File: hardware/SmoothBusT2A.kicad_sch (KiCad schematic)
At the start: 6 parts, among them U1 ATTINY85-20SU, U2 MC7805BDTRKG

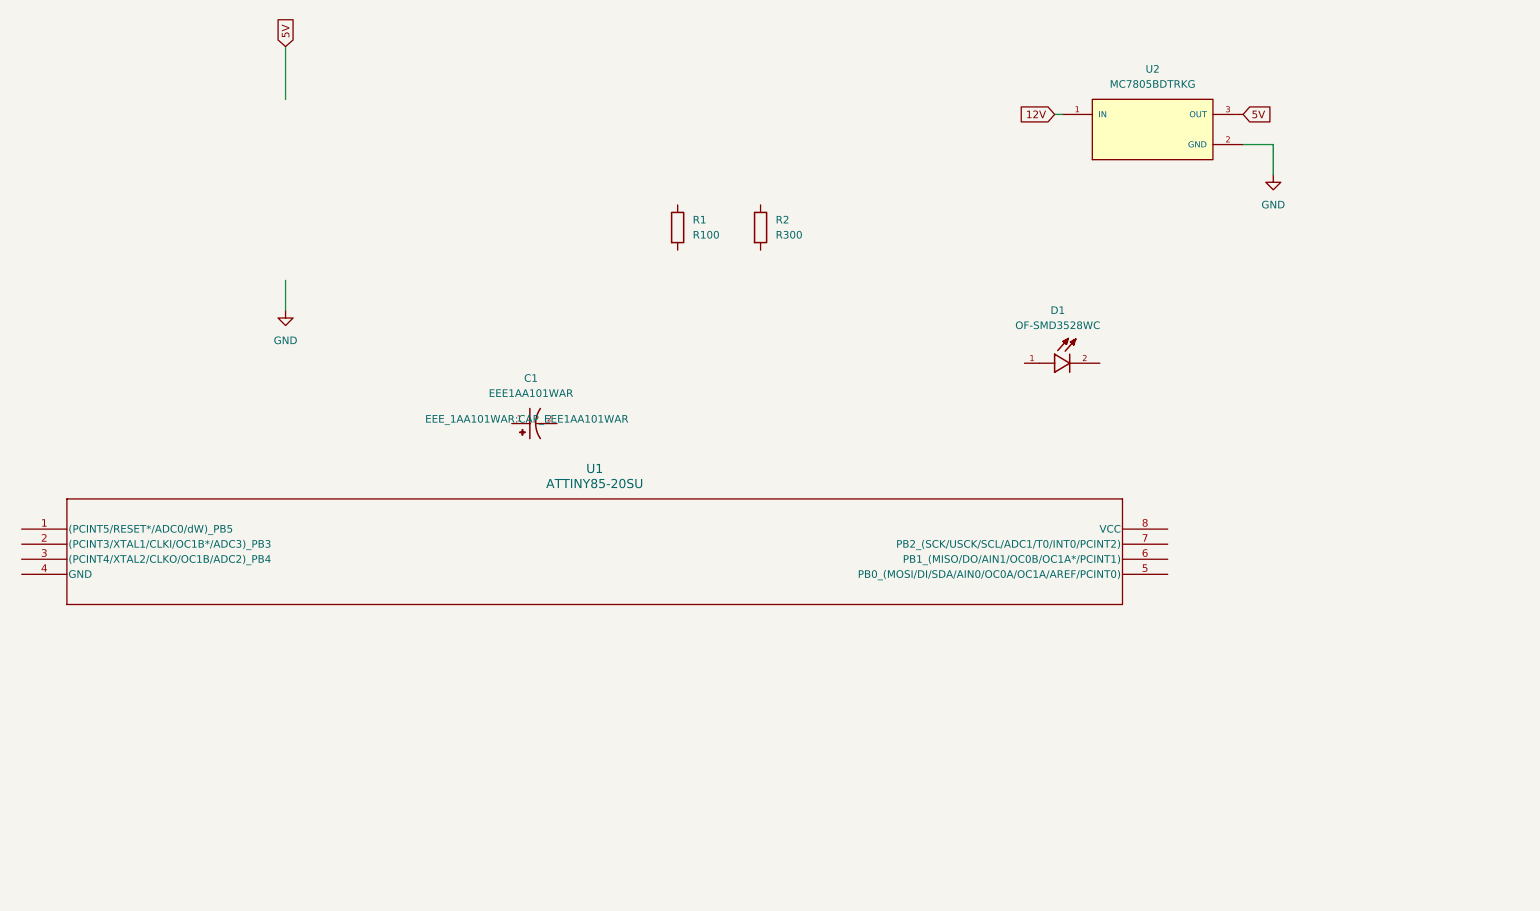
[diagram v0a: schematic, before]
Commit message: added parts to pcb
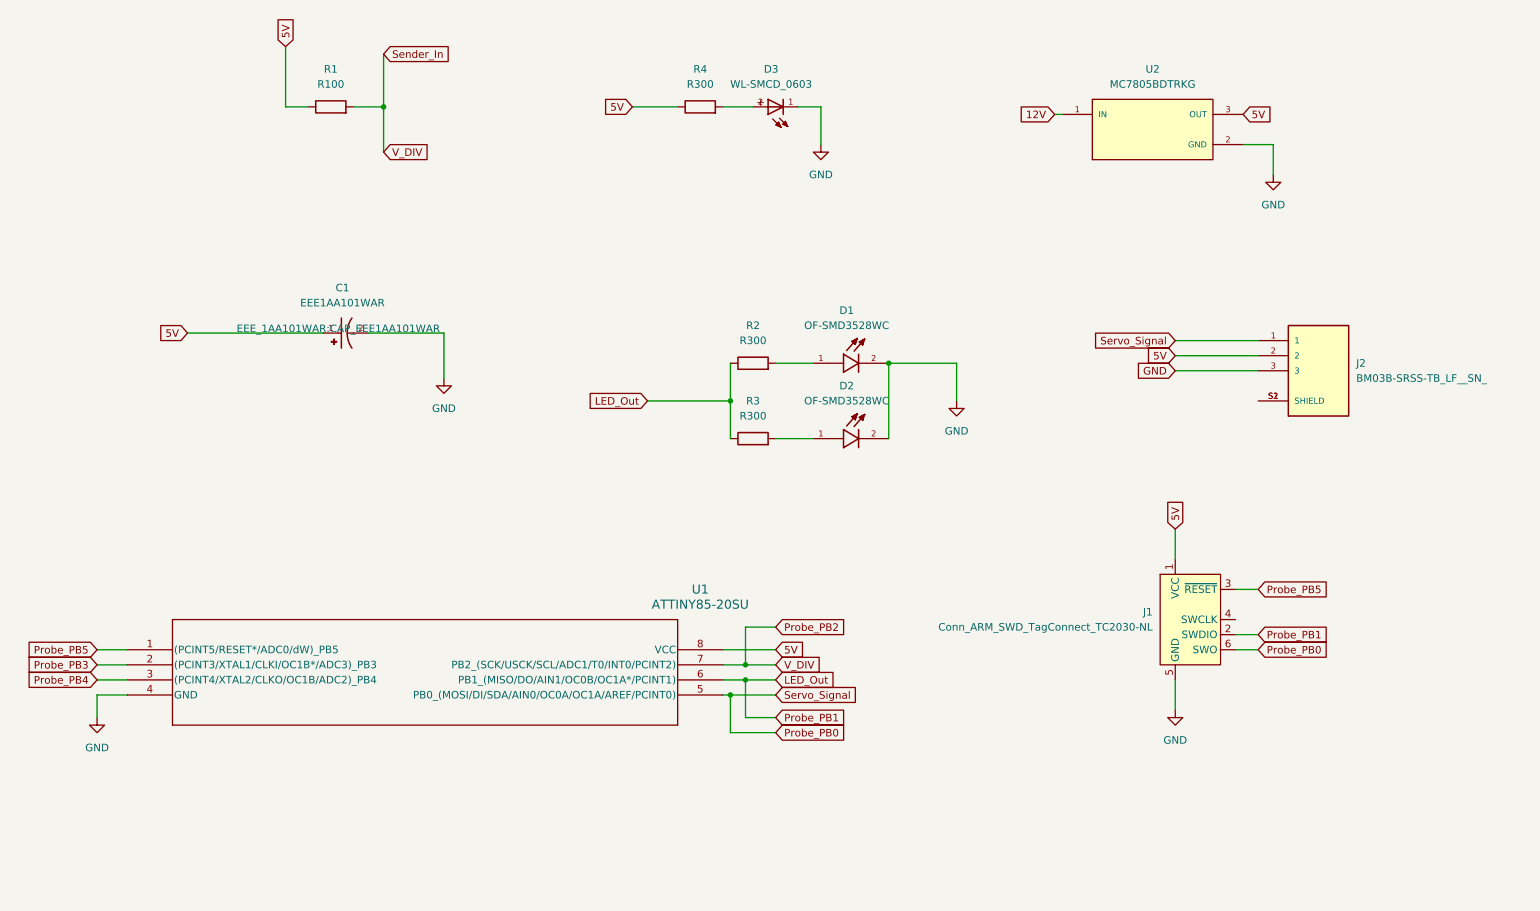
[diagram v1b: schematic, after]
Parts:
- added D2: OF-SMD3528WC, OF-SMD3528WC:LED_OF-SMD3528WC, symbol OF-SMD3528WC:OF-SMD3528WC
- added D3: WL-SMCD_0603, WL-SMCD_0603:WL-SMCD_0603, symbol WL-SMCD_0603:WL-SMCD_0603
- added J1: Conn_ARM_SWD_TagConnect_TC2030-NL, Connector:Tag-Connect_TC2030-IDC-NL_2x03_P1.27mm_Vertical, symbol Connector:Conn_ARM_SWD_TagConnect_TC2030-NL
- added J2: BM03B-SRSS-TB_LF__SN_, BM03B-SRSS-TB_LF__SN_:JST_BM03B-SRSS-TB_LF__SN_, symbol BM03B-SRSS-TB_LF__SN_:BM03B-SRSS-TB_LF__SN_
- added R3, R4: R300, Resistor_SMD:R_0201_0603Metric_Pad0.64x0.40mm_HandSolder, symbol Device:R
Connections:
- net 5V: now also C1.1, R1.1, U1.8 (VCC), J1.1 (VCC), J2.2, R4.1
- net GND: now also C1.2, D1.2, U1.4 (GND), D2.2, D3.1, J1.5 (GND), J2.3
- net Probe_PB2: now reaches R1.2
- net Probe_PB2: now also U1.7 (PB2_(SCK/USCK/SCL/ADC1/T0/INT0/PCINT2))
- net LED_Out: now reaches R2.1
- net LED_Out: now also U1.6 (PB1_(MISO/DO/AIN1/OC0B/OC1A*/PCINT1)), J1.2 (SWDIO), R3.1
- net at R2.2: now also D1.1
- net Probe_PB5: now reaches U1.1 ((PCINT5/RESET*/ADC0/dW)_PB5)
- net Probe_PB5: now also J1.3 (~{RESET})
- net Probe_PB3: now reaches U1.2 ((PCINT3/XTAL1/CLKI/OC1B*/ADC3)_PB3)
- net Probe_PB4: now reaches U1.3 ((PCINT4/XTAL2/CLKO/OC1B/ADC2)_PB4)
- net Probe_PB0: now reaches U1.5 (PB0_(MOSI/DI/SDA/AIN0/OC0A/OC1A/AREF/PCINT0))
- net Probe_PB0: now also J1.6 (SWO), J2.1
- new net: D3.2, R4.2
- new net: D2.1, R3.2
- new net: J2.S1 (SHIELD), J2.S2 (SHIELD)
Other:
- moved on the sheet: C1, D1, R1, R2, U1

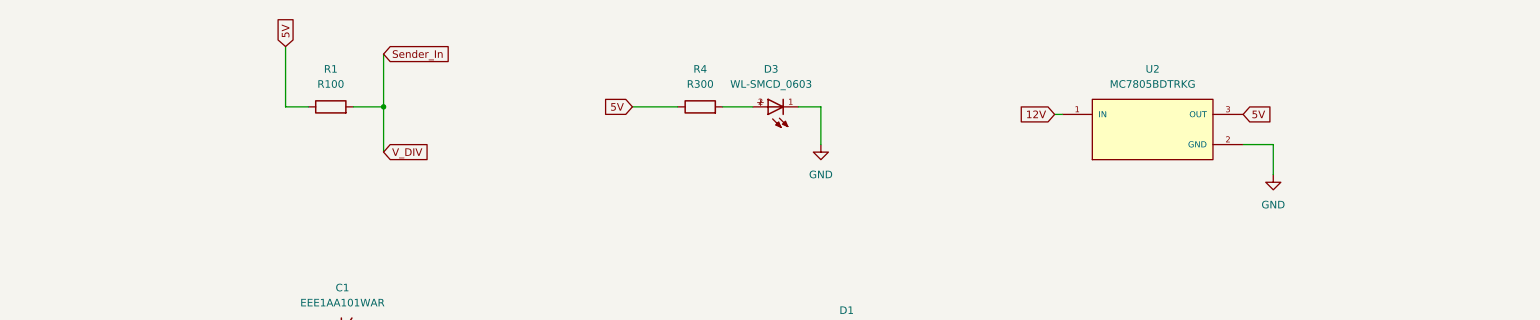
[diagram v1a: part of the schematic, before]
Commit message: routing traces
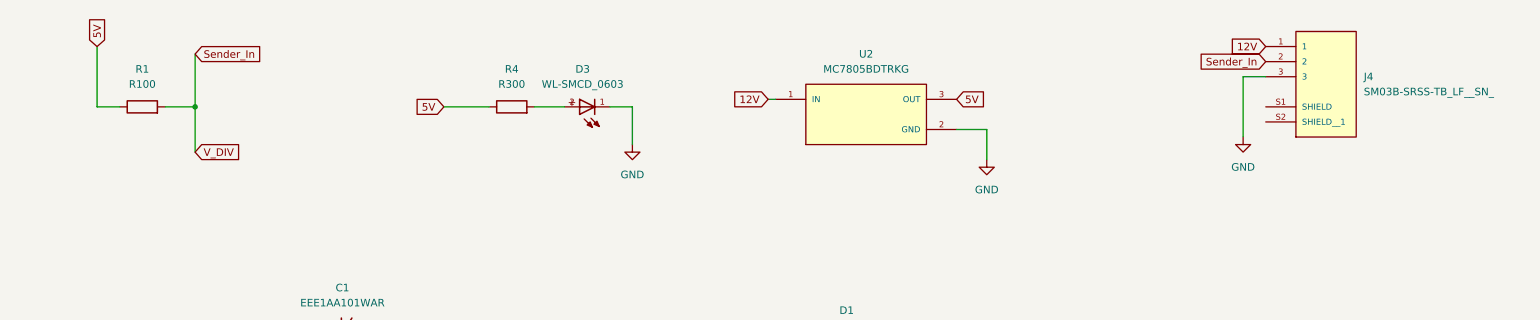
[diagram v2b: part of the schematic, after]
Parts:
- added J4: SM03B-SRSS-TB_LF__SN_, SM03B_SRSS_TB_LF__SN_:JST_SM03B-SRSS-TB_LF__SN_, symbol SM03B-SRSS-TB_LF__SN_:SM03B-SRSS-TB_LF__SN_
- D3: footprint WL-SMCD_0603:WL-SMCD_0603 -> 150060VS55040:WL-SMCD_0603
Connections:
- net 12V: now also J4.1
- net GND: now also J4.3
- net Probe_PB2: now also J4.2
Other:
- moved on the sheet: D3, R1, R4, U2

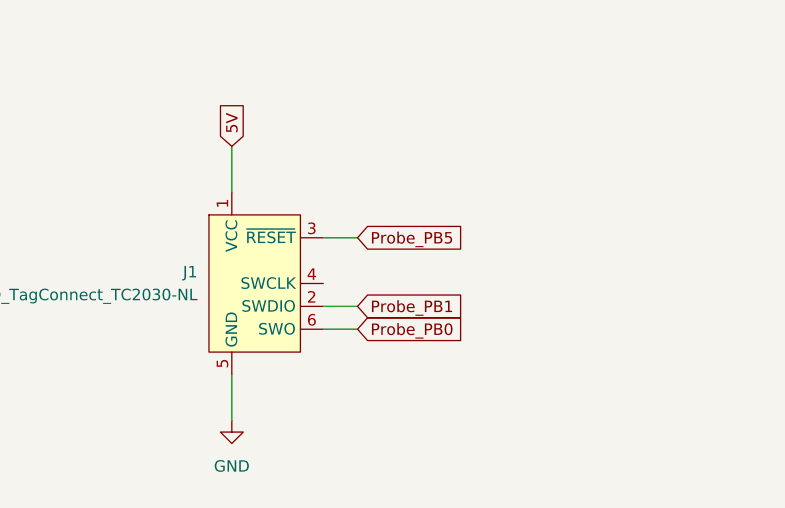
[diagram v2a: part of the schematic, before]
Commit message: finish tracing and add bom
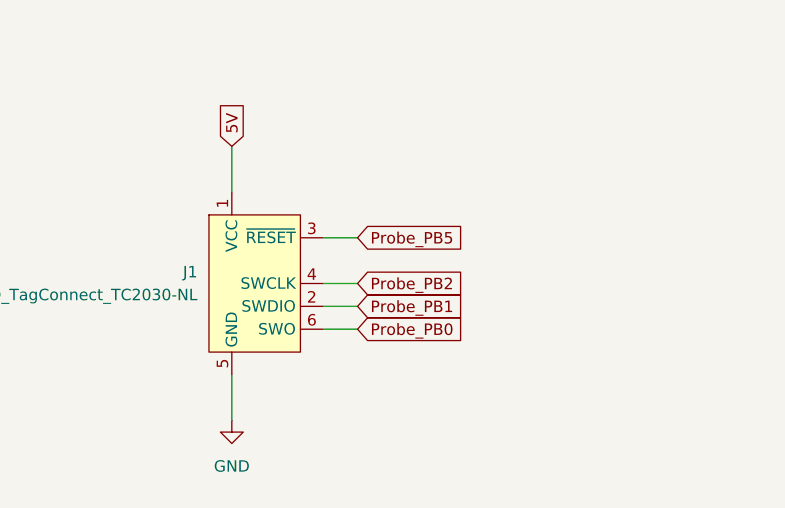
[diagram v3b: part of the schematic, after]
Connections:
- net Probe_PB2: now also J1.4 (SWCLK)

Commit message: version 1
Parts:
- added R5, R6: R10k, Resistor_SMD:R_0201_0603Metric_Pad0.64x0.40mm_HandSolder, symbol Device:R
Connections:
- net GND: now also R5.2, R6.2
- net Probe_PB3: now also R5.1
- net Probe_PB4: now also R6.1
